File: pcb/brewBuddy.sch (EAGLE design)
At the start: 3 parts

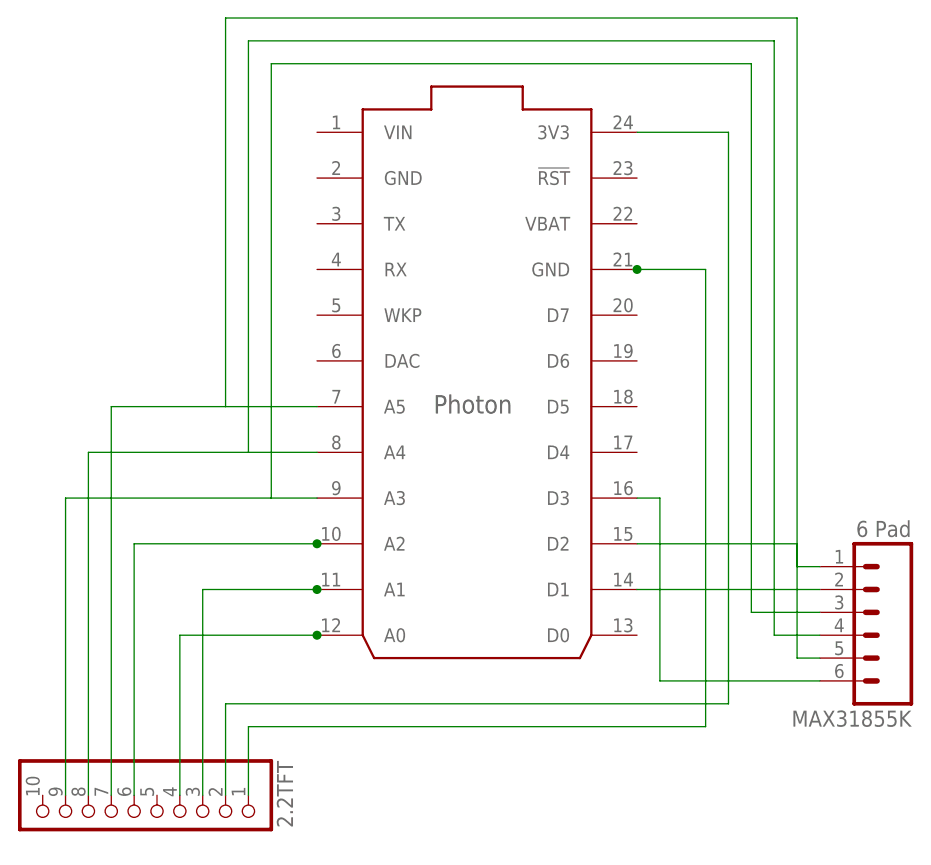
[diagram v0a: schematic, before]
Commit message: modified sketch to show image on startup; tweaked pcb
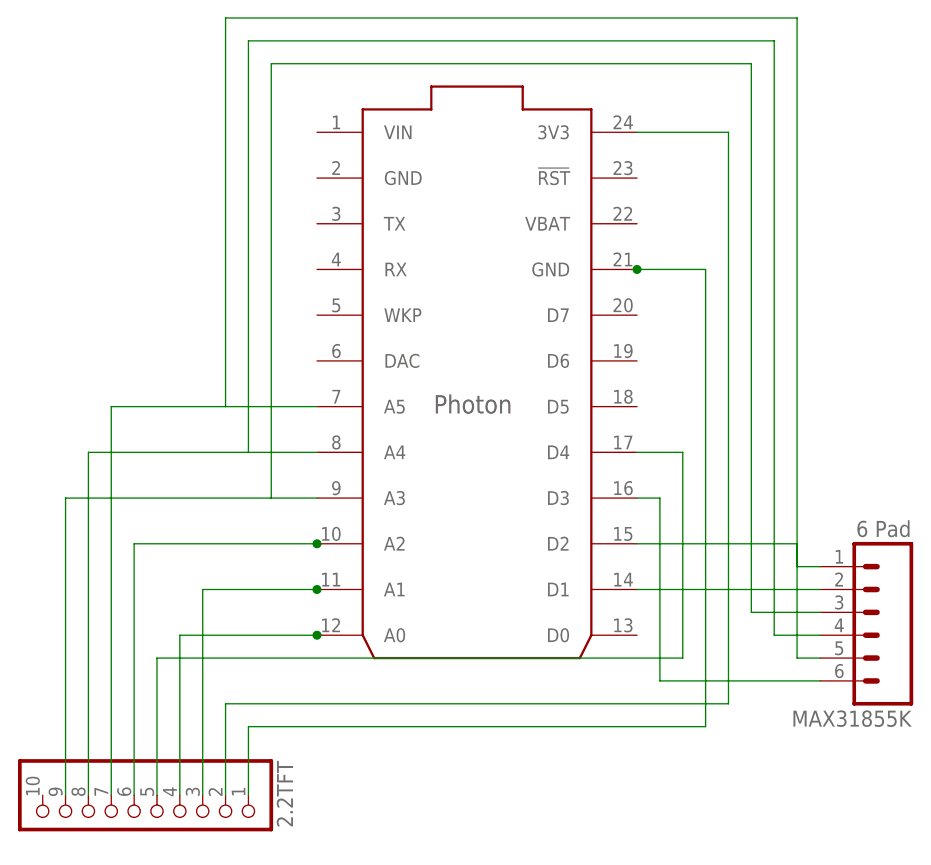
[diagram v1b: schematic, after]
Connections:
- new net N$7: 2.2TFT.5, U$1.D4
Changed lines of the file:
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@@
 <?xml version="1.0" encoding="utf-8"?>
 <!DOCTYPE eagle SYSTEM "eagle.dtd">
-<eagle version="7.6.0">
+<eagle version="7.7.0">
 <drawing>
 <settings>
@@
 </segment>
 </net>
+<net name="N$7" class="0">
+<segment>
+<pinref part="2.2TFT" gate="A" pin="5"/>
+<wire x1="25.4" y1="38.1" x2="25.4" y2="53.34" width="0.1524" layer="91"/>
+<wire x1="25.4" y1="53.34" x2="83.82" y2="53.34" width="0.1524" layer="91"/>
+<wire x1="83.82" y1="53.34" x2="83.82" y2="76.2" width="0.1524" layer="91"/>
+<pinref part="U$1" gate="G$1" pin="D4"/>
+<wire x1="83.82" y1="76.2" x2="78.74" y2="76.2" width="0.1524" layer="91"/>
+</segment>
+</net>
